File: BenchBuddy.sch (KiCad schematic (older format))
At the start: 0 parts

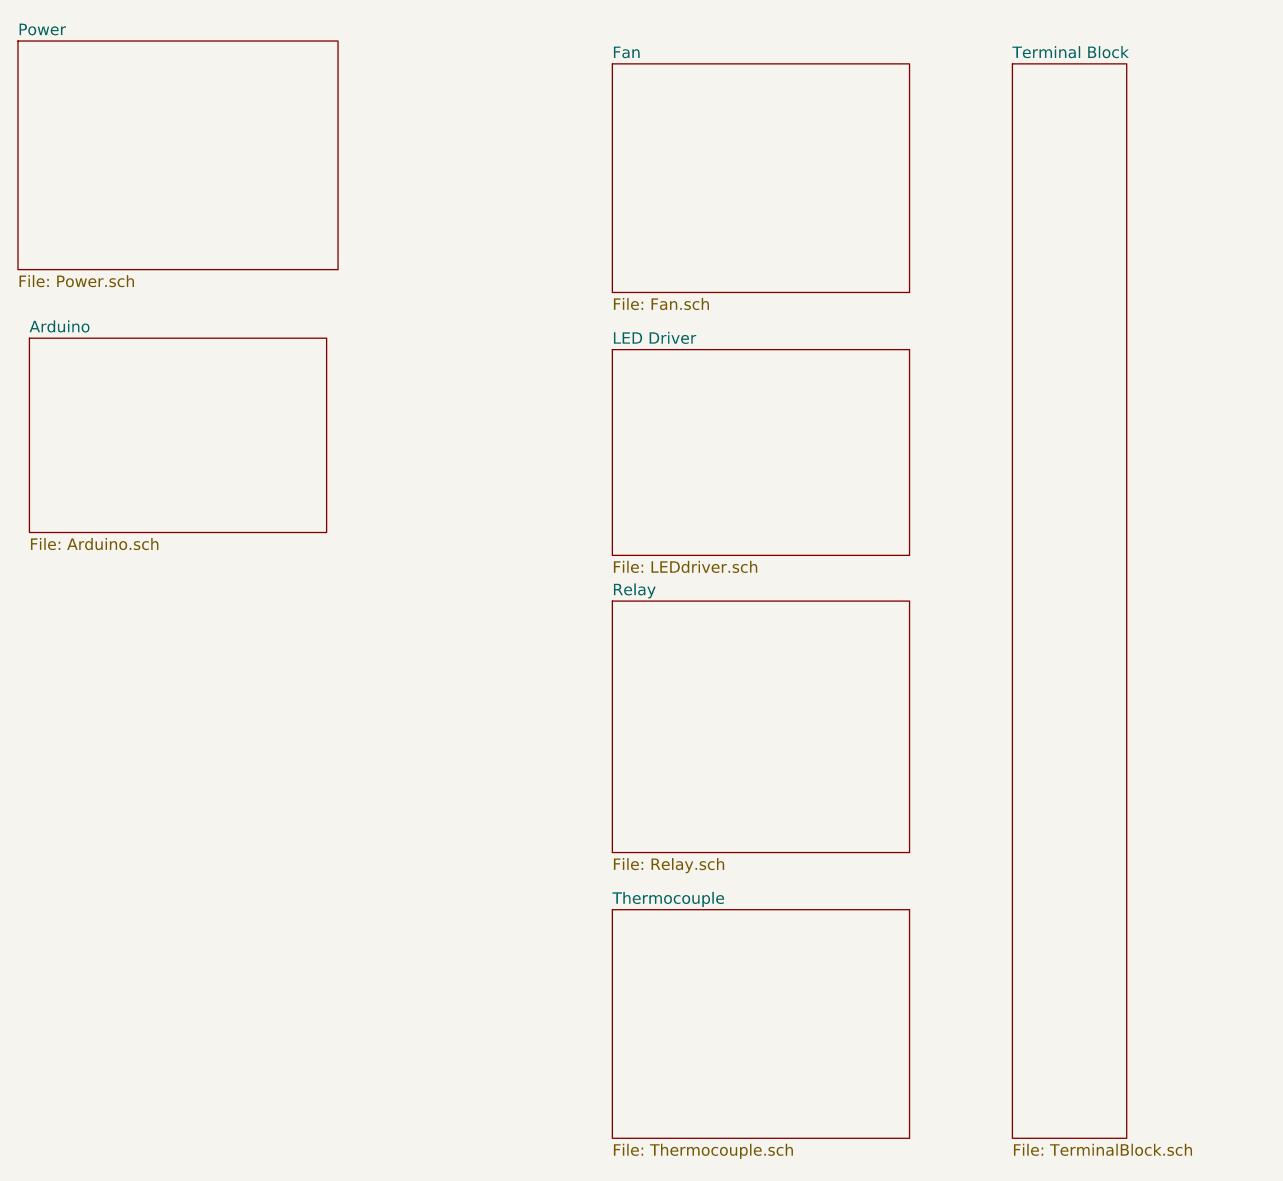
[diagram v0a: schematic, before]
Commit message: added inputs and outputs
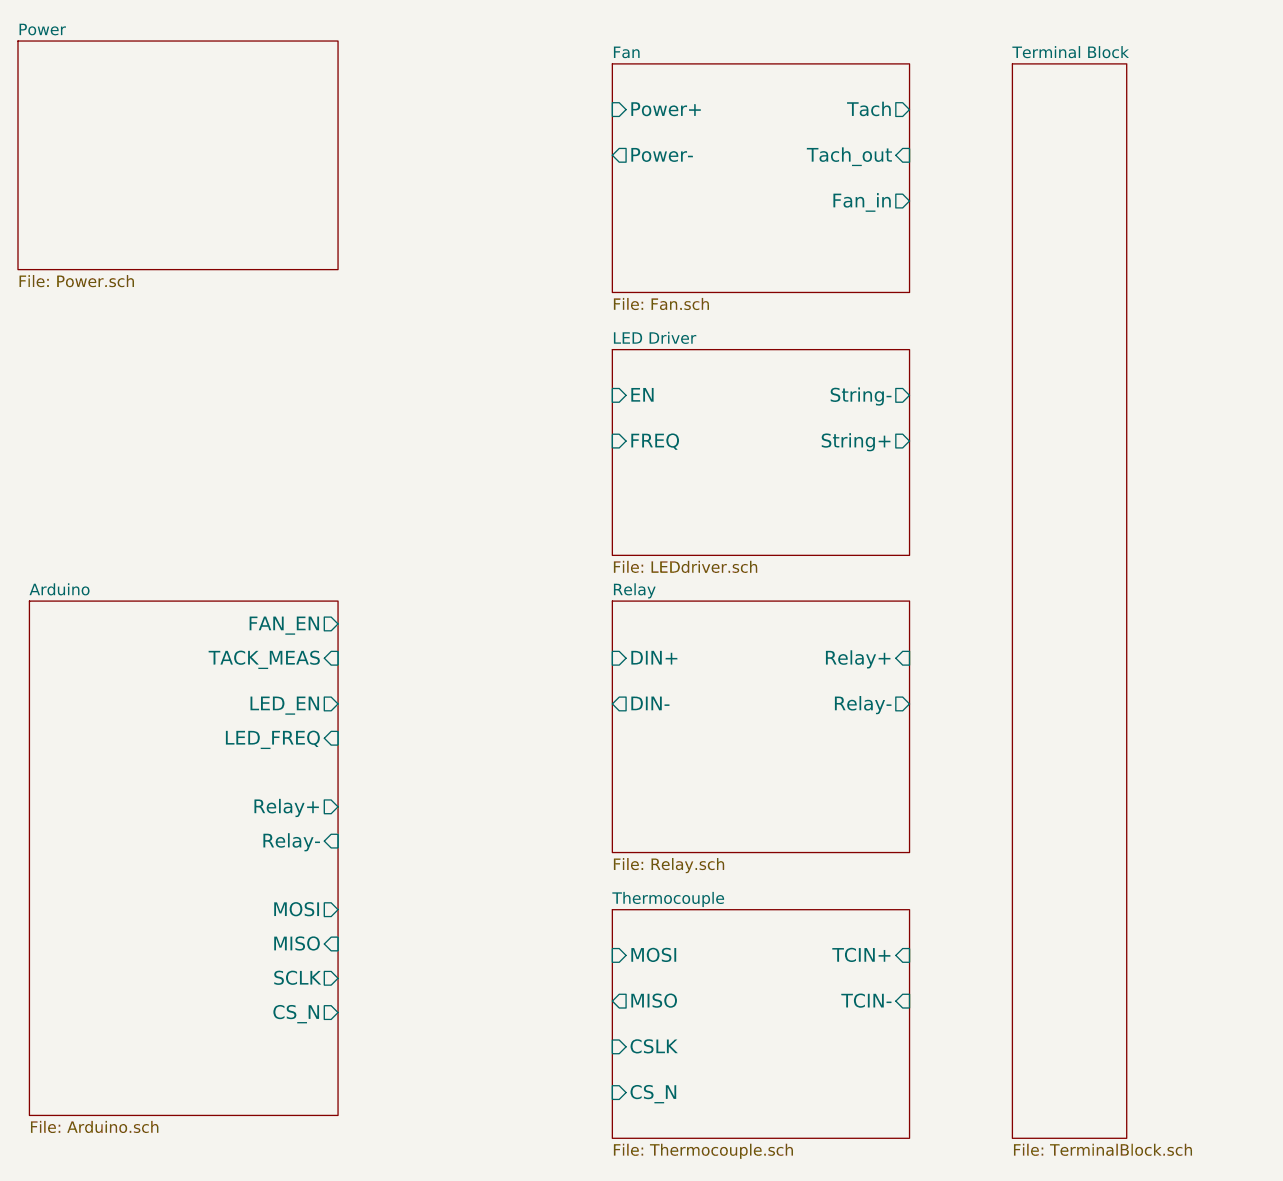
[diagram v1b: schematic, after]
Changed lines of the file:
@@
 $EndDescr
 $Sheet
-S 5500 2300 1300 850
+S 5500 3450 1350 2250
 U 52EC1697
 F0 "Arduino" 50
 F1 "Arduino.sch" 50
+F2 "Relay+" O R 6850 4350 60
+F3 "Relay-" I R 6850 4500 60
+F4 "MOSI" O R 6850 4800 60
+F5 "MISO" I R 6850 4950 60
+F6 "SCLK" O R 6850 5100 60
+F7 "CS_N" O R 6850 5250 60
+F8 "LED_EN" O R 6850 3900 60
+F9 "LED_FREQ" I R 6850 4050 60
+F10 "FAN_EN" O R 6850 3550 60
+F11 "TACK_MEAS" I R 6850 3700 60
 $EndSheet
 $Sheet
@@
 F0 "Relay" 50
 F1 "Relay.sch" 50
+F2 "DIN+" I L 8050 3700 60
+F3 "DIN-" O L 8050 3900 60
+F4 "Relay+" I R 9350 3700 60
+F5 "Relay-" O R 9350 3900 60
 $EndSheet
 $Sheet
@@
 $EndSheet
 $Sheet
-S 8050 2350 1300 900
-U 52EC18A1
-F0 "LED Driver" 50
-F1 "LEDdriver.sch" 50
-$EndSheet
-$Sheet
 S 8050 1100 1300 1000
 U 52EC18BF
 F0 "Fan" 50
 F1 "Fan.sch" 50
+F2 "Power+" I L 8050 1300 60
+F3 "Power-" O L 8050 1500 60
+F4 "Tach" O R 9350 1300 60
+F5 "Tach_out" I R 9350 1500 60
+F6 "Fan_in" O R 9350 1700 60
 $EndSheet
 $Sheet
@@
 F0 "Thermocouple" 50
 F1 "Thermocouple.sch" 50
+F2 "TCIN+" I R 9350 5000 60
+F3 "TCIN-" I R 9350 5200 60
+F4 "MOSI" I L 8050 5000 60
+F5 "MISO" O L 8050 5200 60
+F6 "CSLK" I L 8050 5400 60
+F7 "CS_N" I L 8050 5600 60
+$EndSheet
+$Sheet
+S 8050 2350 1300 900
+U 52EC18A1
+F0 "LED Driver" 50
+F1 "LEDdriver.sch" 50
+F2 "EN" I L 8050 2550 60
+F3 "FREQ" I L 8050 2750 60
+F4 "String-" O R 9350 2550 60
+F5 "String+" O R 9350 2750 60
 $EndSheet
 $EndSCHEMATC
